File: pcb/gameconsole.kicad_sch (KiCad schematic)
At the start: 4 parts

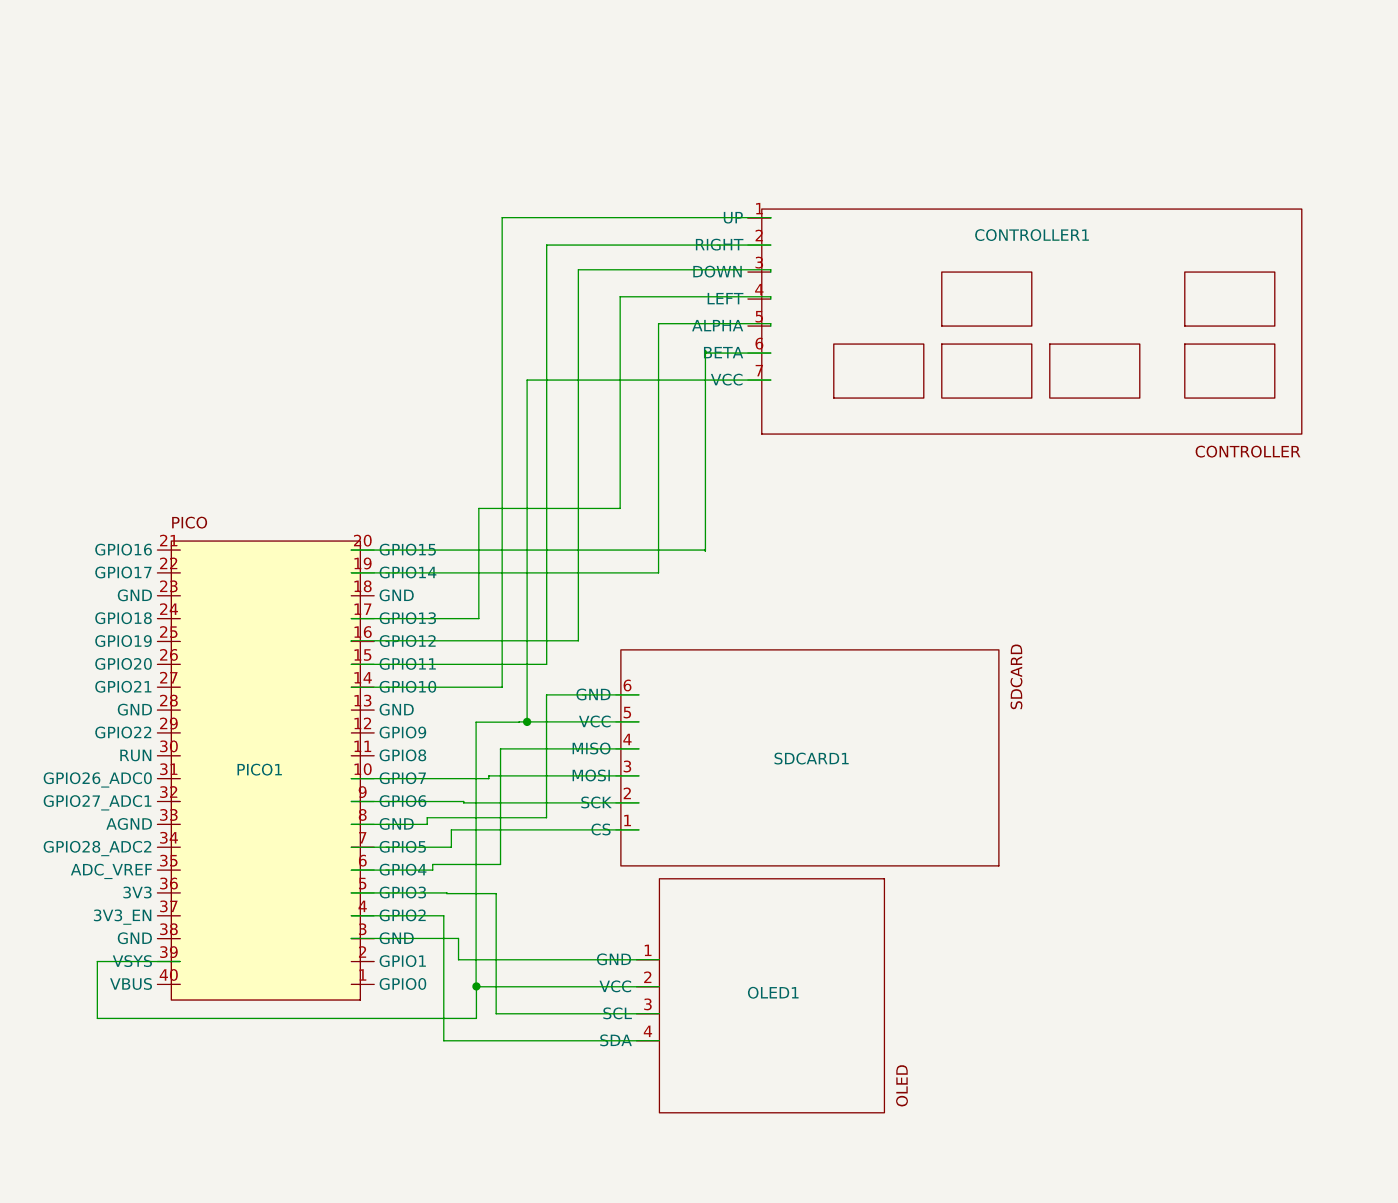
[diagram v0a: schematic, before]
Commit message: Update PCB files
I redesigned the overall footprint to be slimmer, as well as fixed several critical oversights like a component being upside down.
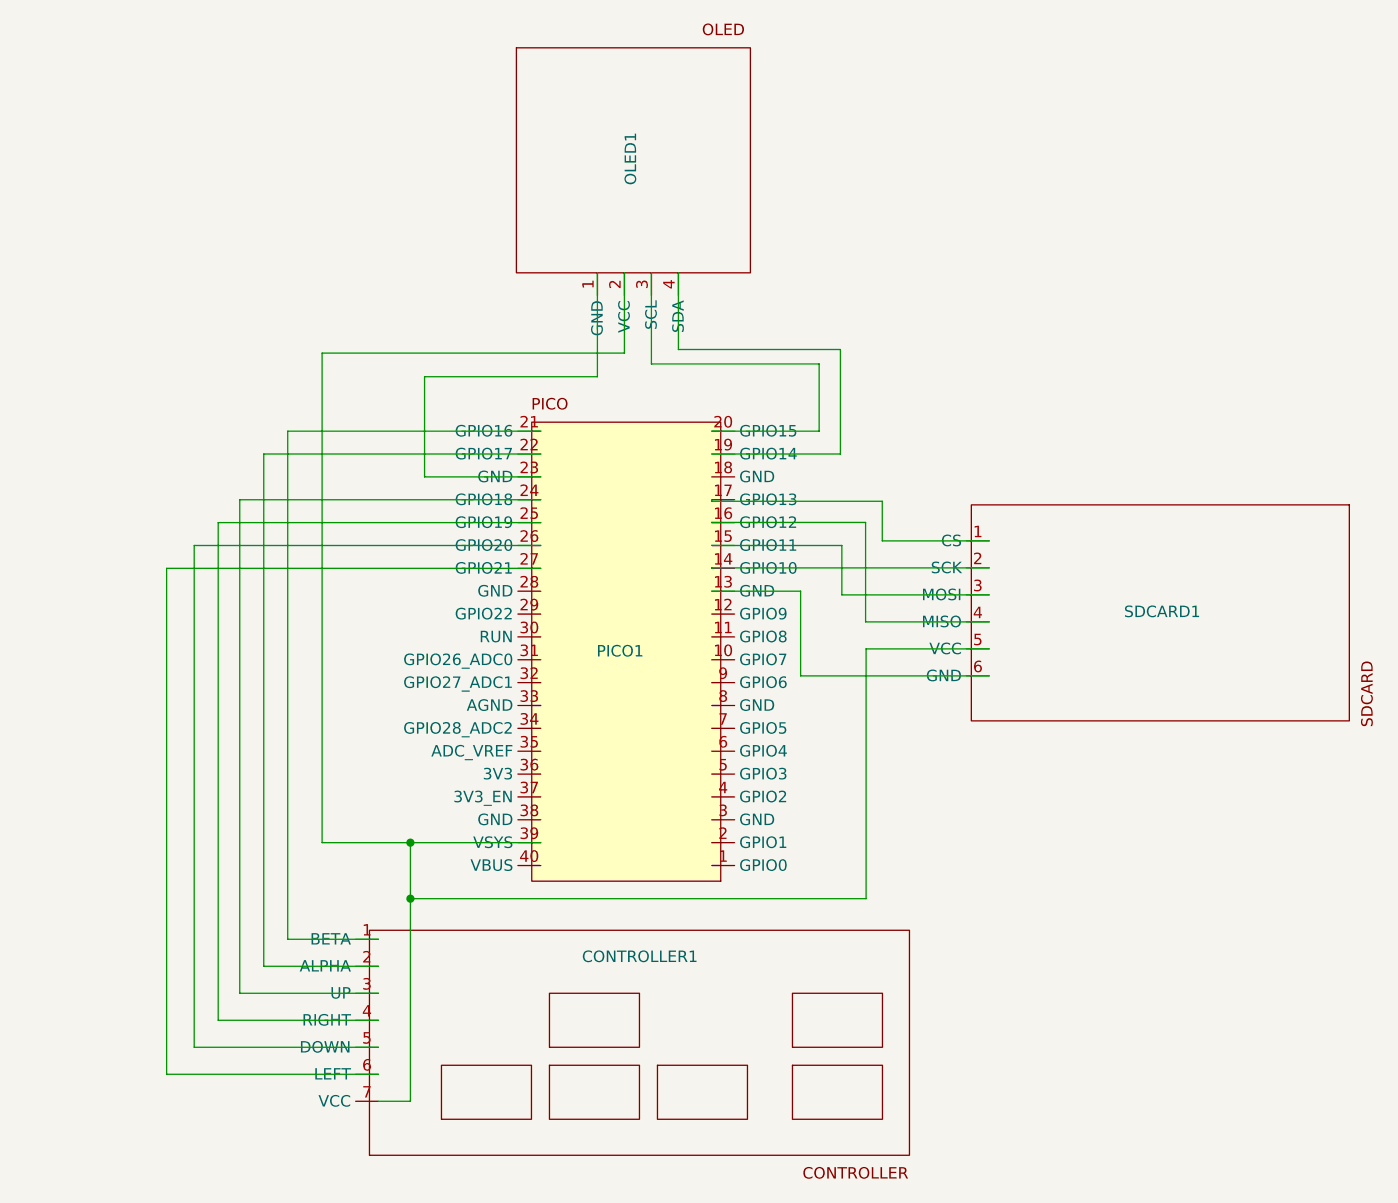
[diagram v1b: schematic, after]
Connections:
- net at SDCARD1.1 (CS): now also PICO1.17 (GPIO13); no longer PICO1.7 (GPIO5)
- net at SDCARD1.2 (SCK): now also PICO1.14 (GPIO10); no longer PICO1.9 (GPIO6)
- net at SDCARD1.3 (MOSI): now also PICO1.15 (GPIO11); no longer PICO1.10 (GPIO7)
- net at SDCARD1.4 (MISO): now also PICO1.16 (GPIO12); no longer PICO1.6 (GPIO4)
- net at SDCARD1.6 (GND): now also PICO1.13 (GND); no longer PICO1.8 (GND)
- net at CONTROLLER1.1 (BETA): now also PICO1.21 (GPIO16); no longer PICO1.14 (GPIO10)
- net at CONTROLLER1.2 (ALPHA): now also PICO1.22 (GPIO17); no longer PICO1.15 (GPIO11)
- net at CONTROLLER1.3 (UP): now also PICO1.24 (GPIO18); no longer PICO1.16 (GPIO12)
- net at CONTROLLER1.4 (RIGHT): now also PICO1.25 (GPIO19); no longer PICO1.17 (GPIO13)
- net at PICO1.19 (GPIO14): now also OLED1.4 (SDA); no longer CONTROLLER1.5 (ALPHA)
- net at PICO1.20 (GPIO15): now also OLED1.3 (SCL); no longer CONTROLLER1.6 (BETA)
- net at PICO1.23 (GND): now also OLED1.1 (GND)
- net at PICO1.26 (GPIO20): now also CONTROLLER1.5 (DOWN)
- net at PICO1.27 (GPIO21): now also CONTROLLER1.6 (LEFT)
- net at PICO1.3 (GND): no longer OLED1.1 (GND)
- net at PICO1.4 (GPIO2): no longer OLED1.4 (SDA)
- net at PICO1.5 (GPIO3): no longer OLED1.3 (SCL)
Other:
- moved on the sheet: CONTROLLER1, OLED1, PICO1, SDCARD1
